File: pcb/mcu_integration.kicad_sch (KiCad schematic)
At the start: 33 parts, among them J1 Conn_01x05, J5 DM3BT-DSF-PEJS, M1 MountingHole_Pad, M2 MountingHole_Pad, M3 MountingHole_Pad, M4 MountingHole_Pad, U1 STM32F103RBTx, U6 LM35DM, Y1 ECS-80-18-5PX-GM-TR

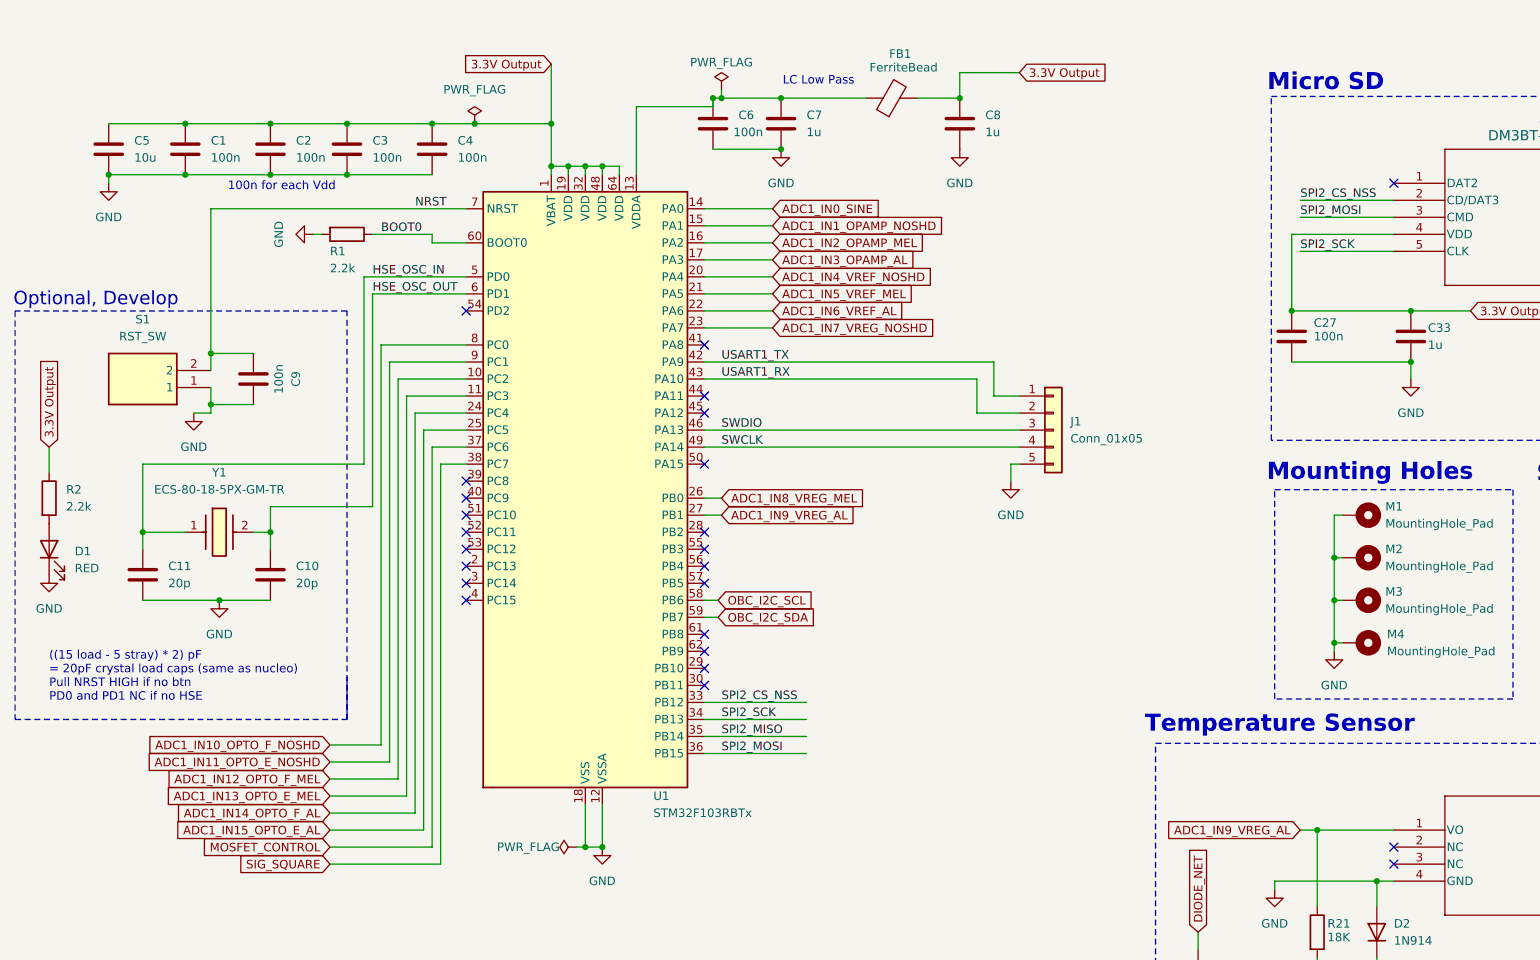
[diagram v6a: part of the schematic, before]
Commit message: Changed IC test orientation
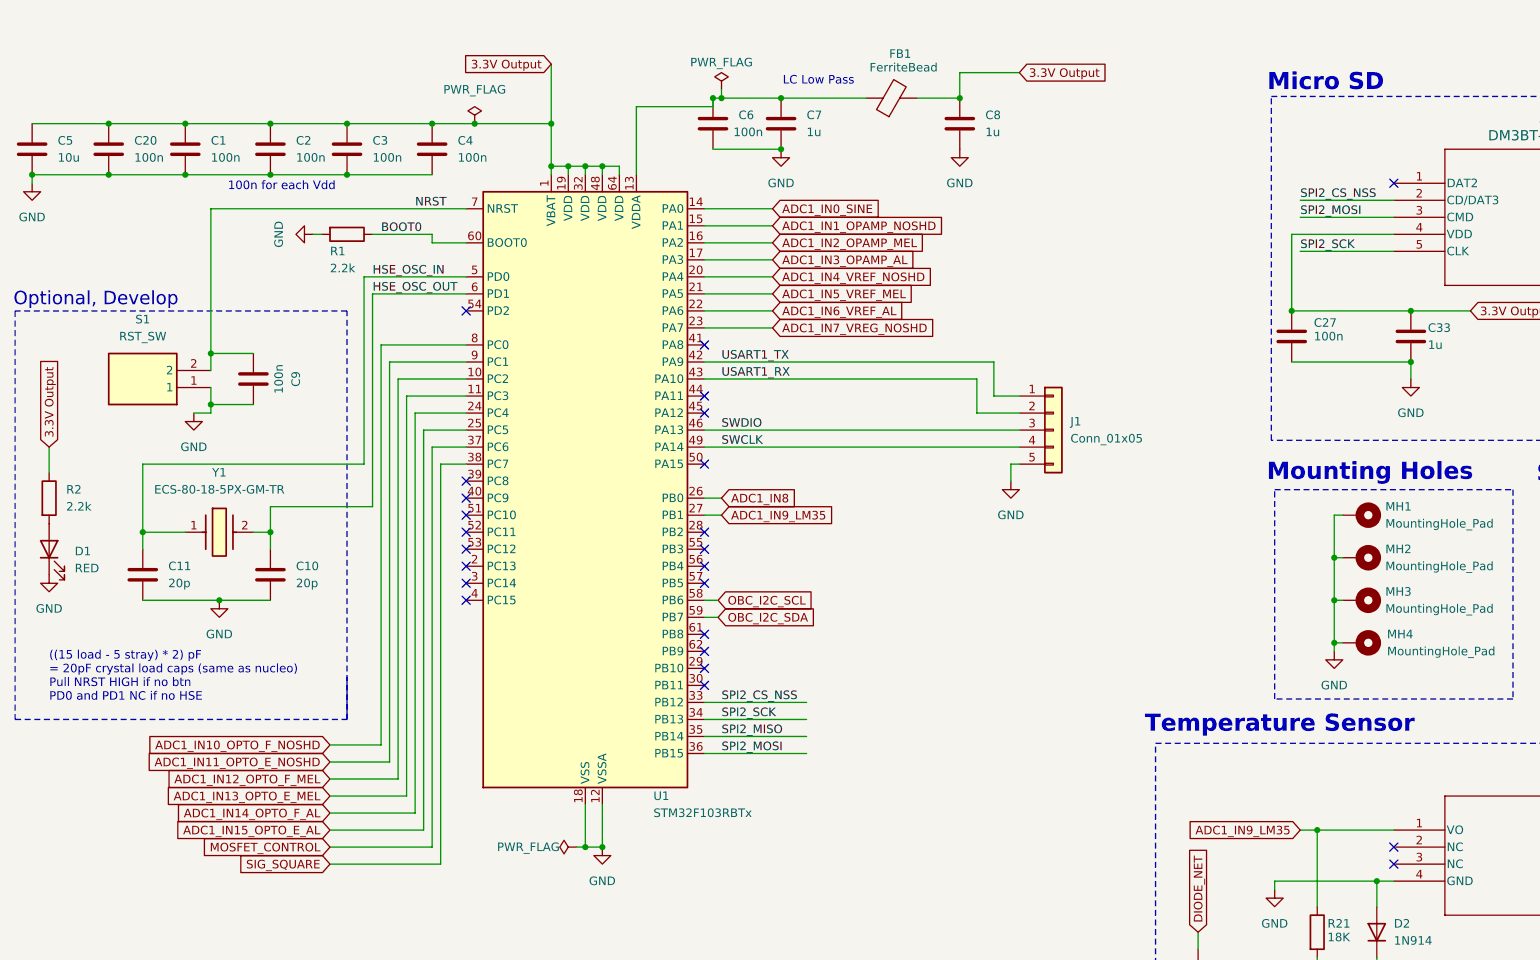
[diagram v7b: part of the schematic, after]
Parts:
- added C20: 100n, Capacitor_SMD:C_0402_1005Metric, symbol Device:C
- MH1: renamed from M1; footprint MountingHole:MountingHole_3.2mm_M3_Pad_Via -> capstone:MountingHole_3.18mm_6.35mm_Pad
- MH2: renamed from M2; footprint MountingHole:MountingHole_3.2mm_M3_Pad_Via -> capstone:MountingHole_3.18mm_6.35mm_Pad
- MH3: renamed from M3; footprint MountingHole:MountingHole_3.2mm_M3_Pad_Via -> capstone:MountingHole_3.18mm_6.35mm_Pad
- MH4: renamed from M4; footprint MountingHole:MountingHole_3.2mm_M3_Pad_Via -> capstone:MountingHole_3.18mm_6.35mm_Pad
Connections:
- net 3.3V Output: now also C20.1
- net GND: now also C20.2
- net ADC1_IN8_VREG_MEL renamed ADC1_IN8
- net ADC1_IN9_VREG_AL renamed ADC1_IN9_LM35
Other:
- moved on the sheet: C5
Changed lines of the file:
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@@
 	)
 	(junction
+		(at 27.94 24.13)
+		(diameter 0)
+		(color 0 0 0 0)
+	)
+	(junction
 		(at 33.02 85.09)
 		(diameter 0)
@@
 	)
 	(junction
+		(at 16.51 31.75)
+		(diameter 0)
+		(color 0 0 0 0)
+	)
+	(junction
 		(at 154.94 20.32)
 		(diameter 0)
@@
 	(wire
 		(pts
-			(xy 27.94 31.75) (xy 39.37 31.75)
-		)
-		(stroke
-			(width 0)
-			(type default)
-		)
-	)
-	(wire
-		(pts
 			(xy 43.18 63.5) (xy 43.18 66.04)
 		)
@@
 	(wire
 		(pts
+			(xy 27.94 24.13) (xy 39.37 24.13)
+		)
+		(stroke
+			(width 0)
+			(type default)
+		)
+	)
+	(wire
+		(pts
 			(xy 60.96 121.92) (xy 71.12 121.92)
 		)
@@
 	(wire
 		(pts
-			(xy 27.94 31.75) (xy 27.94 33.02)
+			(xy 16.51 31.75) (xy 16.51 33.02)
 		)
 		(stroke
@@
 	(wire
 		(pts
-			(xy 27.94 24.13) (xy 39.37 24.13)
+			(xy 16.51 24.13) (xy 27.94 24.13)
 		)
 		(stroke
@@
 	(wire
 		(pts
+			(xy 27.94 31.75) (xy 39.37 31.75)
+		)
+		(stroke
+			(width 0)
+			(type default)
+		)
+	)
+	(wire
+		(pts
 			(xy 66.04 74.93) (xy 33.02 74.93)
 		)
@@
 		)
 	)
+	(wire
+		(pts
+			(xy 16.51 31.75) (xy 27.94 31.75)
+		)
+		(stroke
+			(width 0)
+			(type default)
+		)
+	)
 	(polyline
 		(pts
@@
 		)
 	)
-	(global_label "ADC1_IN9_VREG_AL"
+	(global_label "ADC1_IN9_LM35"
 		(shape input)
 		(at 119.38 82.55 0)
@@
 		)
 		(property "Intersheetrefs" "${INTERSHEET_REFS}"
-			(at 140.1452 82.55 0)
+			(at 137.1818 82.55 0)
 			(effects
 				(font
@@
 		)
 	)
-	(global_label "ADC1_IN8_VREG_MEL"
+	(global_label "ADC1_IN8"
 		(shape input)
 		(at 119.38 80.01 0)
@@
 		)
 		(property "Intersheetrefs" "${INTERSHEET_REFS}"
-			(at 141.657 80.01 0)
+			(at 131.3157 80.01 0)
 			(effects
 				(font
@@
 		)
 	)
-	(global_label "ADC1_IN9_VREG_AL"
+	(global_label "ADC1_IN14_OPTO_F_AL"
 		(shape input)
-		(at 205.74 129.54 180)
+		(at 60.96 127 180)
 		(fields_autoplaced yes)
 		(effects
@@
 		)
 		(property "Intersheetrefs" "${INTERSHEET_REFS}"
-			(at 184.9748 129.54 0)
+			(at 36.8081 127 0)
 			(effects
 				(font
@@
 		)
 	)
-	(global_label "ADC1_IN14_OPTO_F_AL"
+	(global_label "ADC1_IN9_LM35"
 		(shape input)
-		(at 60.96 127 180)
+		(at 205.74 129.54 180)
 		(fields_autoplaced yes)
 		(effects
@@
 		)
 		(property "Intersheetrefs" "${INTERSHEET_REFS}"
-			(at 36.8081 127 0)
+			(at 187.9382 129.54 0)
 			(effects
 				(font
@@
 		(on_board yes)
 		(dnp no)
-		(property "Reference" "M4"
+		(property "Reference" "MH4"
 			(at 218.694 100.33 90)
 			(effects
@@
 			)
 		)
-		(property "Footprint" "MountingHole:MountingHole_3.2mm_M3_Pad_Via"
+		(property "Footprint" "capstone:MountingHole_3.18mm_6.35mm_Pad"
 			(at 214.63 101.6 0)
 			(effects
@@
 			(project "mcu_integration"
 				(path "/c0210bc3-f67f-47d8-a34e-f002a728adb2"
-					(reference "M4")
+					(reference "MH4")
 					(unit 1)
 				)
@@
 	(symbol
 		(lib_id "Device:C")
-		(at 27.94 27.94 0)
+		(at 16.51 27.94 0)
 		(unit 1)
 		(exclude_from_sim no)
@@
 		(fields_autoplaced yes)
 		(property "Reference" "C5"
-			(at 31.75 26.67 0)
+			(at 20.32 26.67 0)
 			(effects
 				(font
@@
 		)
 		(property "Value" "10u"
-			(at 31.75 29.21 0)
+			(at 20.32 29.21 0)
 			(effects
 				(font
@@
 		)
 		(property "Footprint" "Capacitor_SMD:C_0603_1608Metric"
-			(at 28.9052 31.75 0)
+			(at 17.4752 31.75 0)
 			(effects
 				(font
@@
 		)
 		(property "Datasheet" "~"
-			(at 27.94 27.94 0)
+			(at 16.51 27.94 0)
 			(effects
 				(font
@@
 		)
 		(property "Description" ""
-			(at 27.94 27.94 0)
+			(at 16.51 27.94 0)
 			(effects
 				(font
@@
 		(dnp no)
 		(fields_autoplaced yes)
-		(property "Reference" "M2"
+		(property "Reference" "MH2"
 			(at 218.44 87.6299 90)
 			(effects
@@
 			)
 		)
-		(property "Footprint" "MountingHole:MountingHole_3.2mm_M3_Pad_Via"
+		(property "Footprint" "capstone:MountingHole_3.18mm_6.35mm_Pad"
 			(at 214.63 88.9 0)
 			(effects
@@
 			(project "mcu_integration"
 				(path "/c0210bc3-f67f-47d8-a34e-f002a728adb2"
-					(reference "M2")
+					(reference "MH2")
 					(unit 1)
 				)
@@
 		(dnp no)
 		(fields_autoplaced yes)
-		(property "Reference" "M3"
+		(property "Reference" "MH3"
 			(at 218.44 93.9799 90)
 			(effects
@@
 			)
 		)
-		(property "Footprint" "MountingHole:MountingHole_3.2mm_M3_Pad_Via"
+		(property "Footprint" "capstone:MountingHole_3.18mm_6.35mm_Pad"
 			(at 214.63 95.25 0)
 			(effects
@@
 			(project "mcu_integration"
 				(path "/c0210bc3-f67f-47d8-a34e-f002a728adb2"
-					(reference "M3")
+					(reference "MH3")
+					(unit 1)
+				)
+			)
+		)
+	)
+	(symbol
+		(lib_id "Device:C")
+		(at 27.94 27.94 0)
+		(unit 1)
+		(exclude_from_sim no)
+		(in_bom yes)
+		(on_board yes)
+		(dnp no)
+		(fields_autoplaced yes)
+		(property "Reference" "C20"
+			(at 31.75 26.67 0)
+			(effects
+				(font
+					(size 1.27 1.27)
+				)
+				(justify left)
+			)
+		)
+		(property "Value" "100n"
+			(at 31.75 29.21 0)
+			(effects
+				(font
+					(size 1.27 1.27)
+				)
+				(justify left)
+			)
+		)
+		(property "Footprint" "Capacitor_SMD:C_0402_1005Metric"
+			(at 28.9052 31.75 0)
+			(effects
+				(font
+					(size 1.27 1.27)
+				)
+				(hide yes)
+			)
+		)
+		(property "Datasheet" "~"
+			(at 27.94 27.94 0)
+			(effects
+				(font
+					(size 1.27 1.27)
+				)
+				(hide yes)
+			)
+		)
+		(property "Description" ""
+			(at 27.94 27.94 0)
+			(effects
+				(font
+					(size 1.27 1.27)
+				)
+				(hide yes)
+			)
+		)
+		(pin "1"
+		)
+		(pin "2"
+		)
+		(instances
+			(project "mcu_integration"
+				(path "/c0210bc3-f67f-47d8-a34e-f002a728adb2"
+					(reference "C20")
 					(unit 1)
 				)
@@
 	(symbol
 		(lib_id "power:GND")
-		(at 27.94 33.02 0)
+		(at 16.51 33.02 0)
 		(unit 1)
 		(exclude_from_sim no)
@@
 		(fields_autoplaced yes)
 		(property "Reference" "#PWR03"
-			(at 27.94 39.37 0)
+			(at 16.51 39.37 0)
 			(effects
 				(font
@@
 		)
 		(property "Value" "GND"
-			(at 27.94 38.1 0)
+			(at 16.51 38.1 0)
 			(effects
 				(font
@@
 		)
 		(property "Footprint" ""
-			(at 27.94 33.02 0)
+			(at 16.51 33.02 0)
 			(effects
 				(font
@@
 		)
 		(property "Datasheet" ""
-			(at 27.94 33.02 0)
+			(at 16.51 33.02 0)
 			(effects
 				(font
@@
 		)
 		(property "Description" ""
-			(at 27.94 33.02 0)
+			(at 16.51 33.02 0)
 			(effects
 				(font
@@
 		(dnp no)
 		(fields_autoplaced yes)
-		(property "Reference" "M1"
+		(property "Reference" "MH1"
 			(at 218.44 81.2799 90)
 			(effects
@@
 			)
 		)
-		(property "Footprint" "MountingHole:MountingHole_3.2mm_M3_Pad_Via"
+		(property "Footprint" "capstone:MountingHole_3.18mm_6.35mm_Pad"
 			(at 214.63 82.55 0)
 			(effects
@@
 			(project "mcu_integration"
 				(path "/c0210bc3-f67f-47d8-a34e-f002a728adb2"
-					(reference "M1")
+					(reference "MH1")
 					(unit 1)
 				)

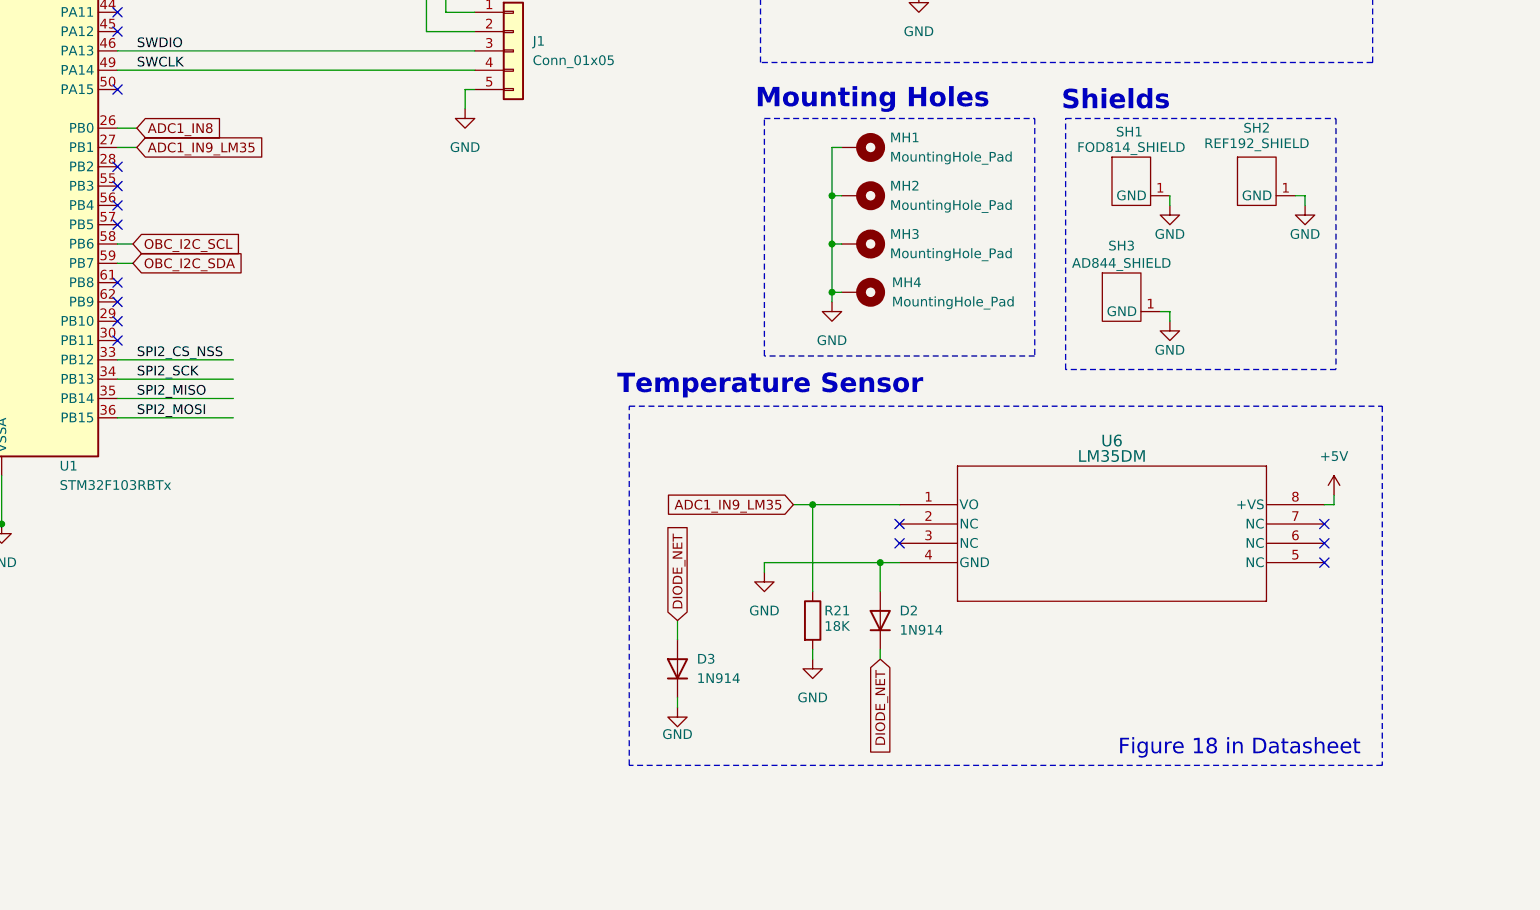
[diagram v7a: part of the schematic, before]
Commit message: Replaced LM35 temp sensor with LMT87
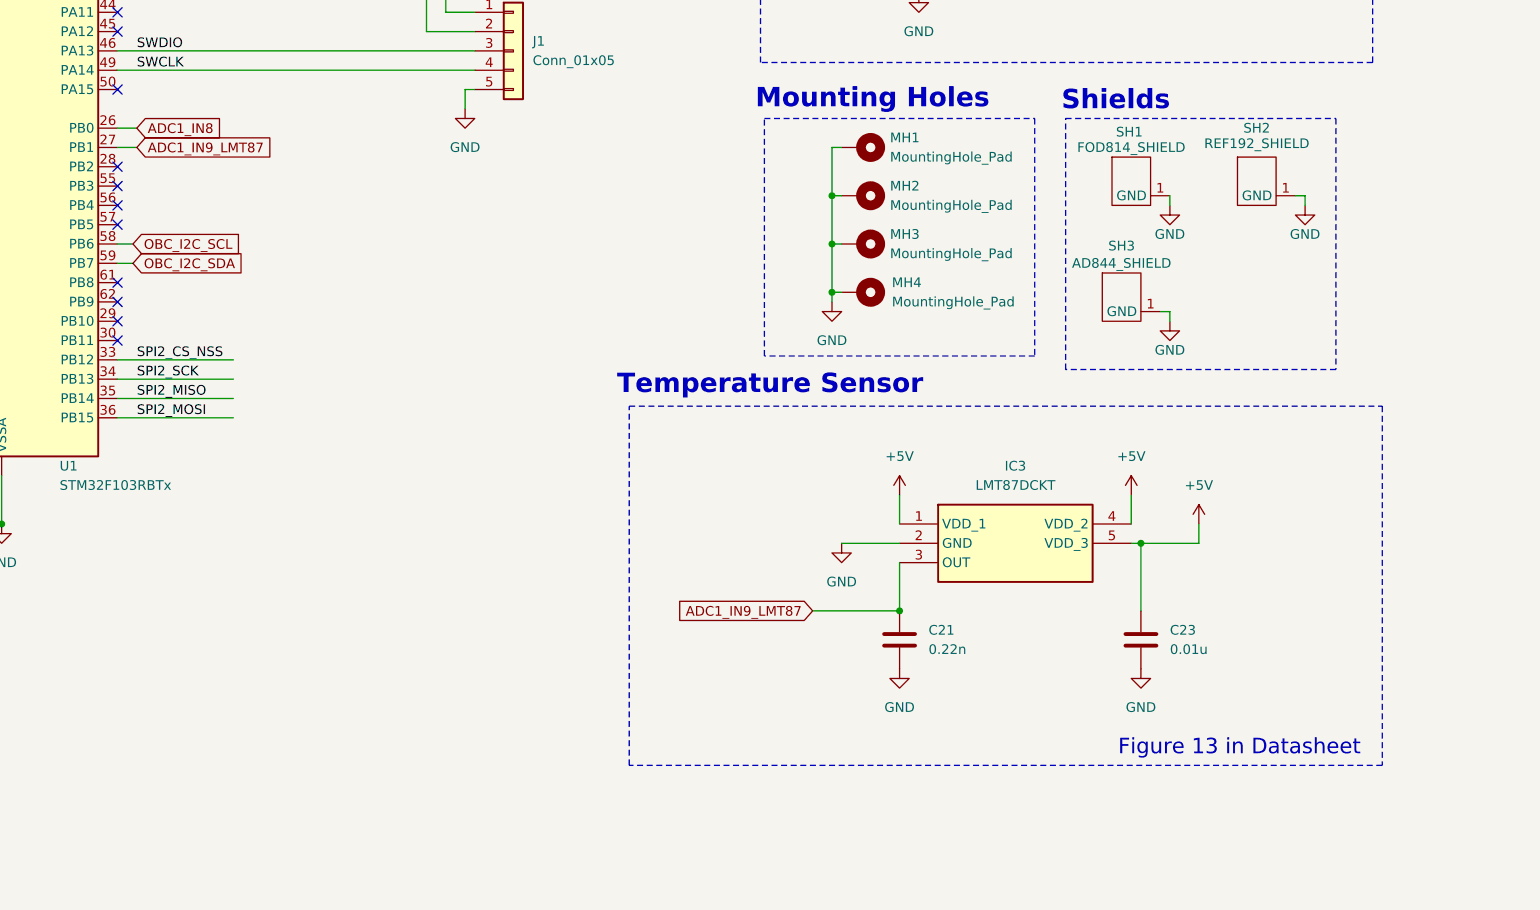
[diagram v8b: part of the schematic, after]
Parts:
- removed D2, D3: 1N914, capstone:SOD-323_1P7X1P25_ONS, symbol Device:D
- removed R21: 18K, Resistor_SMD:R_0402_1005Metric, symbol Device:R
- removed U6: LM35DM, capstone:LM35DM, symbol capstone:LM35DM
- added C21: 0.22n, Capacitor_SMD:C_0402_1005Metric, symbol Device:C
- added C23: 0.01u, Capacitor_SMD:C_0402_1005Metric, symbol Device:C
- added IC3: LMT87DCKT, SamacSys_Parts:SOT65P210X110-5N, symbol SamacSys_Parts:LMT87DCKT
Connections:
- net +5V: now also C23.1, IC3.1 (VDD_1), IC3.4 (VDD_2), IC3.5 (VDD_3)
- net GND: now also C21.2, C23.2, IC3.2 (GND)
- net ADC1_IN9_LM35 renamed ADC1_IN9_LMT87
- net ADC1_IN9_LMT87: now also C21.1, IC3.3 (OUT)
- no-connect marks 30 -> 25
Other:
- note added: "Figure 13 in Datasheet"
- note removed: "Figure 18 in Datasheet"
